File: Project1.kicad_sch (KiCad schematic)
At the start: 16 parts, among them J1 48037-0001, U1 MCP1702T-3302E/CB, U2 MCP6022T-I/ST

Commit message: Add report and necessary files
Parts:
- removed J1: 48037-0001, 480370001:MOLEX_48037-0001, symbol 480370001:48037-0001
- removed U1: MCP1702T-3302E/CB, MCP1702T_WITHPIN:MCP1702T-3302E&slash_CB, symbol MCP1702T_WITHPIN:MCP1702T-3302E/CB
- removed U2: MCP6022T-I/ST, MCP6022T-I_WITHPIN:MCP6022T-I&slash_ST, symbol MCP6022T-I_WITHPIN:MCP6022T-I/ST
- added J?: 48037-0001, MOLEX_48037-0001, symbol 48037-0001:48037-0001
- added U1: MCP1702T-3302E/CB, SOT-23A_MC_MCH, symbol MCP1702T-3302E/CB:MCP1702T-3302E/CB
- added U2: MCP6022T-I/ST, TSSOP8_MC_MCH, symbol MCP6022T-I/ST:MCP6022T-I/ST
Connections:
- net GND: now also U1.1 (GND), U2.4 (VSS)
- net PWR_USB: now also U1.3 (VIN)
- net VIN_NEG_AMP2: now also U2.6 (VINB-)
- net VIN_POS_AMP1: now also U2.3 (VINA+)
- net VIN_POS_AMP2: now also U2.5 (VINB+)
- net VOUT_AMP1: now also U2.1 (VOUTA), U2.2 (VINA-)
- net VOUT_AMP2: now also U2.7 (VOUTB)
- net VOUT_REG: now also U1.2 (VOUT), U2.8 (VDD)
- new net: J?.S1 (SHIELD), J?.S2 (SHIELD)

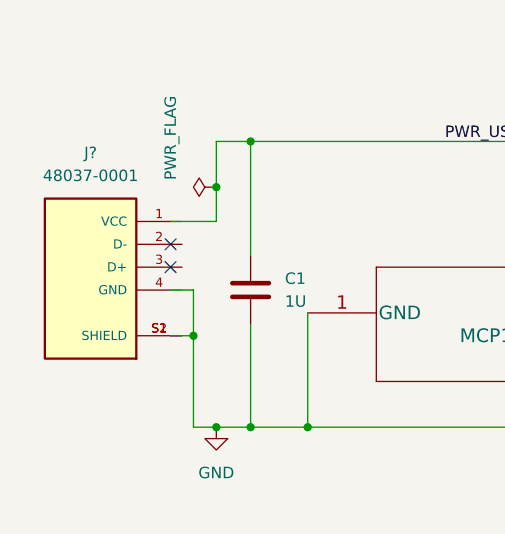
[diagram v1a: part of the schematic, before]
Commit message: Fix schematic errors
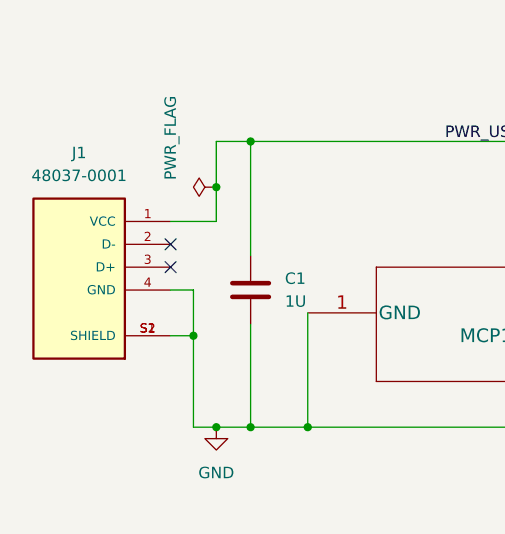
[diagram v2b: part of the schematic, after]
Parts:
- gave numbers to parts that had none: 1
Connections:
- net GND: now also J1.4 (GND), J1.S1 (SHIELD), J1.S2 (SHIELD)
- net PWR_USB: now also J1.1 (VCC)
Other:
- moved on the sheet: J1
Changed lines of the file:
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@@
     (pin "2")
   )
-  (symbol (lib_id "48037-0001:48037-0001") (at 21.59 53.34 0) (mirror y) (unit 1)
-    (in_bom yes) (on_board yes) (fields_autoplaced)
-    (property "Reference" "J?" (id 0) (at 21.59 40.64 0))
-    (property "Value" "48037-0001" (id 1) (at 21.59 43.18 0))
-    (property "Footprint" "MOLEX_48037-0001" (id 2) (at 21.59 48.26 0)
-      (effects (font (size 1.27 1.27)) (justify left bottom) hide)
-    )
-    (property "Datasheet" "" (id 3) (at 21.59 53.34 0)
-      (effects (font (size 1.27 1.27)) (justify left bottom) hide)
-    )
-    (property "STANDARD" "Manufacturer Recommendations" (id 4) (at 17.78 59.69 0)
-      (effects (font (size 1.27 1.27)) (justify left bottom) hide)
-    )
-    (property "MAXIMUM_PACKAGE_HEIGHT" "4.6mm" (id 5) (at 12.7 54.61 0)
-      (effects (font (size 1.27 1.27)) (justify left bottom) hide)
-    )
-    (property "MANUFACTURER" "Molex" (id 6) (at 12.7 52.07 0)
-      (effects (font (size 1.27 1.27)) (justify left bottom) hide)
-    )
-    (property "PARTREV" "D" (id 7) (at 21.59 53.34 0)
+  (symbol (lib_id "48037-0001:48037-0001") (at 20.32 53.34 0) (mirror y) (unit 1)
+    (in_bom yes) (on_board yes) (fields_autoplaced)
+    (property "Reference" "J1" (id 0) (at 20.32 40.64 0))
+    (property "Value" "48037-0001" (id 1) (at 20.32 43.18 0))
+    (property "Footprint" "MOLEX_48037-0001" (id 2) (at 20.32 48.26 0)
+      (effects (font (size 1.27 1.27)) (justify left bottom) hide)
+    )
+    (property "Datasheet" "" (id 3) (at 20.32 53.34 0)
+      (effects (font (size 1.27 1.27)) (justify left bottom) hide)
+    )
+    (property "STANDARD" "Manufacturer Recommendations" (id 4) (at 16.51 59.69 0)
+      (effects (font (size 1.27 1.27)) (justify left bottom) hide)
+    )
+    (property "MAXIMUM_PACKAGE_HEIGHT" "4.6mm" (id 5) (at 11.43 54.61 0)
+      (effects (font (size 1.27 1.27)) (justify left bottom) hide)
+    )
+    (property "MANUFACTURER" "Molex" (id 6) (at 11.43 52.07 0)
+      (effects (font (size 1.27 1.27)) (justify left bottom) hide)
+    )
+    (property "PARTREV" "D" (id 7) (at 20.32 53.34 0)
       (effects (font (size 1.27 1.27)) (justify left bottom) hide)
     )
@@
     )
     (path "/20c2ed21-766b-4288-9040-83feecefb662"
-      (reference "J?") (unit 1) (value "48037-0001") (footprint "MOLEX_48037-0001")
+      (reference "J1") (unit 1) (value "48037-0001") (footprint "MOLEX_48037-0001")
     )
     (path "/d6c43bfe-b9e4-4f53-bacf-98602496dd5f"
